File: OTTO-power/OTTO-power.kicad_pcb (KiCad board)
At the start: 2 copper layers, 68.5 x 20.5 mm, 30 parts, among them J1 Signals, J2 5v, J3 battery, J4 USB_B_Micro, M1 FS8205, SW1 ON_OFF_SWITCH, U1 TP4056, U2 FS312F-G, U3 MT3608

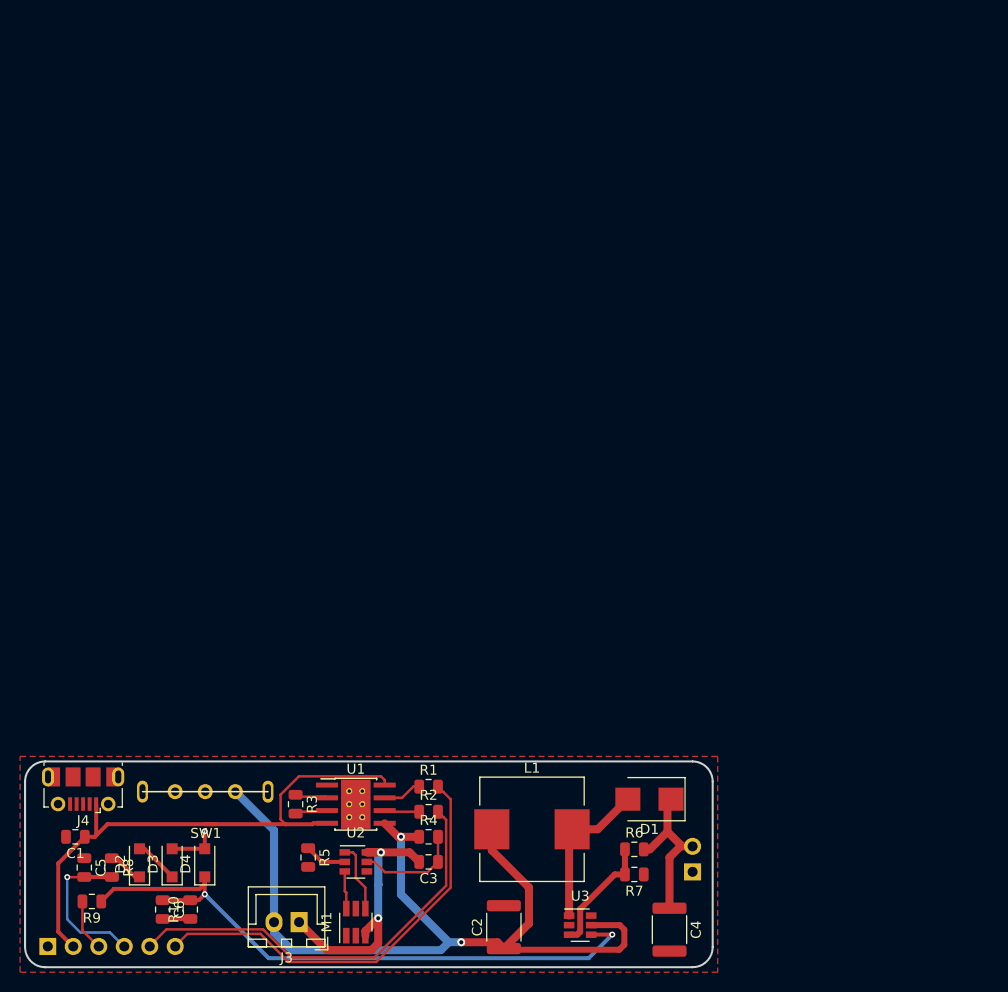
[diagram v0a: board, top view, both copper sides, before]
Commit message: new board, need to route the DC connector (and make a protection circuit between it and the usb)
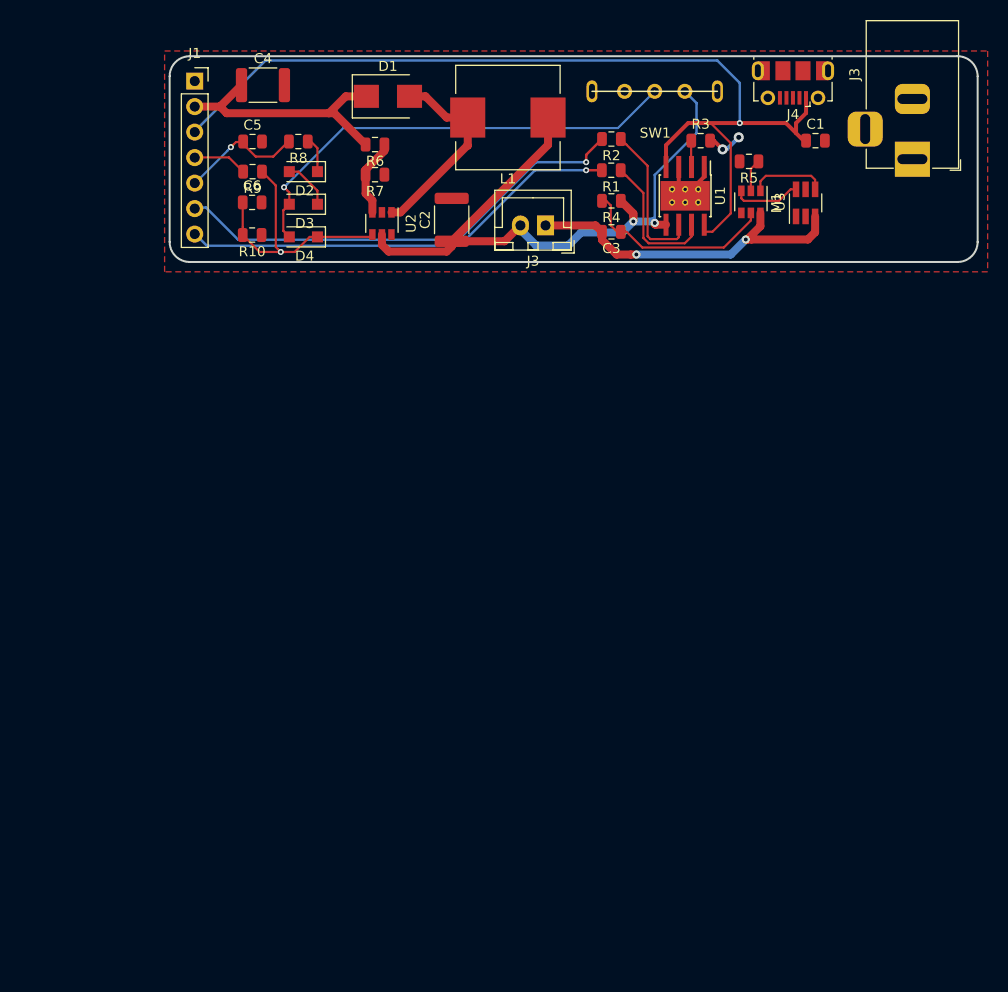
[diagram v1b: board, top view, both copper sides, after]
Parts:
- removed J2: 5v, Connector_PinHeader_2.54mm:PinHeader_1x02_P2.54mm_Vertical
- removed the J3 at (206.7, 170.4)
- added J3: battery, Connector_JST:JST_XH_B02B-XH-A_1x02_P2.50mm_Vertical, F.Cu at (231.2, 101.0)
- added J3: Barrel_Jack, Connector_BarrelJack:BarrelJack_Horizontal, F.Cu at (267.8, 94.4)
- J1: value Signals -> Conn_01x07; footprint Connector_PinHeader_2.54mm:PinHeader_1x06_P2.54mm_Vertical -> Connector_PinSocket_2.54mm:PinSocket_1x07_P2.54mm_Vertical; moved to F.Cu
- R3: value 2k -> 1.2k
- U2: value FS312F-G -> MT3608
- U3: value MT3608 -> FS312F-G
- moved C1 101.2 mm to (258.1, 92.6), turned to 0 degrees
- moved J4 99.8 mm to (255.9, 86.8)
- moved C4 93.4 mm to (203.1, 87.0), turned to 0 degrees
- moved J1 87.4 mm to (196.3, 86.6), turned to 0 degrees
- moved M1 84.5 mm to (257.2, 98.8)
- moved SW1 82.9 mm to (242.1, 87.6)
- moved R5 82.1 mm to (251.5, 94.6), turned to 180 degrees
- moved R3 77.5 mm to (246.7, 92.6), turned to 0 degrees
- moved R6 74.8 mm to (214.3, 92.9), turned to 180 degrees
- moved D1 74.7 mm to (215.6, 88.1), turned to 0 degrees
- moved R8 74.7 mm to (206.6, 92.6), turned to 180 degrees
- moved R9 74.5 mm to (202.1, 95.6)
- moved R7 74.4 mm to (214.3, 95.9)
- moved C5 74.3 mm to (202.1, 92.6), turned to 0 degrees
- moved U3 74.0 mm to (251.7, 98.7), turned to 270 degrees
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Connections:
- C2 pad 1: BATT -> +BATT
- C5 pad 1: GNDREF -> SENSE_PIN
- C5 pad 2: SENSE_PIN -> GNDREF
- J1 pad 2: LED_POW -> 5V
- J1 pad 3: OUT_PIN -> LED_POW
- J1 pad 4: SENSE_PIN -> OUT_PIN
- J1 pad 5: LED_G -> SENSE_PIN
- J1 pad 6: LED_R -> LED_G
- L1 pad 1: BATT -> +BATT
- R4 pad 1: BATT -> +BATT
- SW1 pad 3: BATT -> +BATT
- U1 pad 5: BATT -> +BATT
- U2 pad 1: Net-(M1-Pad4) -> Net-(D1-Pad2)
- U2 pad 2: Net-(R5-Pad1) -> GNDREF
- U2 pad 3: Net-(M1-Pad6) -> Net-(R6-Pad1)
- U2 pad 4: Net-(U2-Pad4) -> EN
- U2 pad 5: Net-(C3-Pad1) -> +BATT
- U2 pad 6: -BATT -> Net-(U2-Pad6)
- U3 pad 1: Net-(D1-Pad2) -> Net-(M1-Pad4)
- U3 pad 2: GNDREF -> Net-(R5-Pad1)
- U3 pad 3: Net-(R6-Pad1) -> Net-(M1-Pad6)
- U3 pad 4: EN -> Net-(U3-Pad4)
- U3 pad 5: BATT -> Net-(C3-Pad1)
- U3 pad 6: Net-(U3-Pad6) -> -BATT
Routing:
- net BATT: track 88.3 -> 0.00 mm, vias 2 -> 0
- net +BATT: track 0.00 -> 67.5 mm, vias 0 -> 2
- net Net-(D3-Pad2): track 5.00 -> 46.5 mm
- net LED_POW: track 56.6 -> 97.8 mm, vias 0 -> 1
- net EN: track 64.2 -> 26.4 mm, vias 2 -> 1
- net Net-(R2-Pad1): track 3.49 -> 15.3 mm
- net Net-(R1-Pad1): track 3.90 -> 14.2 mm
- net 5V: track 16.3 -> 26.0 mm
- net Net-(C3-Pad1): track 10.4 -> 19.8 mm
- net -BATT: track 27.3 -> 34.4 mm
- net Net-(D1-Pad2): track 15.1 -> 19.8 mm
- net GNDREF: track 6.00 -> 10.5 mm, vias 0 -> 2
- net LED_G: track 42.1 -> 46.5 mm, vias 0 -> 1
- net Net-(R6-Pad1): track 11.9 -> 7.84 mm
- net Net-(M1-Pad6): track 3.71 -> 6.78 mm
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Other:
- board size 68.5 x 20.5 mm -> 80.5 x 20.5 mm

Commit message: started working on the mainboard
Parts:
- removed the J3 at (267.8, 94.4)
- added REF**: MountingHole_2.5mm, MountingHole:MountingHole_2.5mm, F.Cu at (269.3, 87.1)
- added REF**: MountingHole_2.5mm, MountingHole:MountingHole_2.5mm, F.Cu at (214.8, 87.1)
- added REF**: MountingHole_2.5mm, MountingHole:MountingHole_2.5mm, F.Cu at (269.3, 101.6)
- moved D1 6.90 mm to (222.4, 88.1)
- moved C1 6.00 mm to (264.1, 92.6)
- moved C2 6.00 mm to (227.9, 100.4)
- moved C3 6.00 mm to (243.8, 101.6)
- moved C5 6.00 mm to (208.1, 92.6)
- moved C6 6.00 mm to (208.0, 98.7)
- moved D2 6.00 mm to (213.1, 95.6)
- moved D3 6.00 mm to (213.1, 98.9)
- moved D4 6.00 mm to (213.1, 102.1)
- moved J1 6.00 mm to (202.3, 86.6)
- moved J3 6.00 mm to (237.2, 101.0)
- moved L1 6.00 mm to (233.5, 90.2)
- moved M1 6.00 mm to (263.2, 98.8)
- moved R1 6.00 mm to (243.8, 95.5)
- moved R10 6.00 mm to (208.0, 102.0)
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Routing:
- net Net-(D1-Pad2): track 19.8 -> 18.9 mm
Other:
- board size 80.5 x 20.5 mm -> 72.5 x 20.5 mm
